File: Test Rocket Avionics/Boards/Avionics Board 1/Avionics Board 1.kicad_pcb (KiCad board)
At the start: 4 copper layers, 50 x 50 mm, 57 parts, among them J1 USB_A, J14 1S LiPo, J2 1S LiPo, M2.5 CHASSIS_GND, U1 ECS-.327-12.5-17X-TR, U2 SPX3819M5-L-3-3, U3 ATSAMD21G18, U4 MCP73831, U5 MPL3115A2, U6 DS3231-SO16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

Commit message: Update some stuff
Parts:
- added C20: 2.2u, Capacitors_SMD:C_1206, B.Cu at (44.4, 120.7)
- added C21: 1u, Capacitors_SMD:C_0805, F.Cu at (34.5, 123.1)
- added C22: 220p, Capacitors_SMD:C_0805, B.Cu at (44.0, 112.9)
- added C6: 2.2u, Capacitors_SMD:C_1206, B.Cu at (38.1, 117.5)
- added D6: D, Diodes_SMD:D_SOD-123F, B.Cu at (38.2, 120.4)
- added J3: EXPANSION_HEADER, Pin_Headers:Pin_Header_Straight_2x10_Pitch1.00mm, F.Cu at (24.2, 110.7)
- added J4: USB_A, Connectors:USB_Mini-B, B.Cu at (45.2, 84.9)
- added J5: SERVO, Pin_Headers:Pin_Header_Straight_1x03_Pitch2.54mm, F.Cu at (34.2, 119.9)
- added L1: 10u, Inductors_SMD:L_Wuerth_HCI-5040, B.Cu at (43.3, 124.6)
- added R17: 10k, Resistors_SMD:R_0805, B.Cu at (46.2, 117.5)
- added R18: 51k, Resistors_SMD:R_0805, B.Cu at (41.8, 113.0)
- added R19: 13.3k, Resistors_SMD:R_0805, B.Cu at (46.2, 114.0)
- added U10: NC7WZ07, TO_SOT_Packages_SMD:SOT-363_SC-70-6, F.Cu at (44.5, 111.1)
- added U11: LMR62014, TO_SOT_Packages_SMD:SOT-23-5, B.Cu at (42.8, 117.5)
- C14: value C -> 220p
- moved J2 54.2 mm to (29.4, 98.5), turned to 270 degrees
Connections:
- C14 pad 1: GND -> Net-(C14-Pad1)
- C14 pad 2: +3V3 -> /6V_SERVO_SUPPLY
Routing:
- net GND: track 80.8 -> 107.5 mm, vias 32 -> 34
- net /D13: track 0.00 -> 26.1 mm, vias 0 -> 1
- net /MISO: track 0.00 -> 23.0 mm
- net /D11: track 0.00 -> 22.6 mm, vias 0 -> 1
- net /SWCLK: track 6.41 -> 28.9 mm, vias 0 -> 2
- net /SWDIO: track 5.80 -> 26.7 mm, vias 0 -> 2
- net +3V3: track 54.3 -> 75.0 mm, vias 14 -> 16
- net /SCK: track 0.00 -> 19.8 mm, vias 0 -> 1
- net /MOSI: track 0.00 -> 18.6 mm
- net /6V_SERVO_SUPPLY: track 0.00 -> 18.1 mm
- net /A5: track 2.82 -> 20.0 mm, vias 0 -> 2
- net Net-(J5-Pad1): track 0.00 -> 16.3 mm
- net /A1: track 0.00 -> 11.2 mm, vias 0 -> 1
- net /D10: track 0.00 -> 9.32 mm
- net /A2: track 0.00 -> 8.78 mm, vias 0 -> 1
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
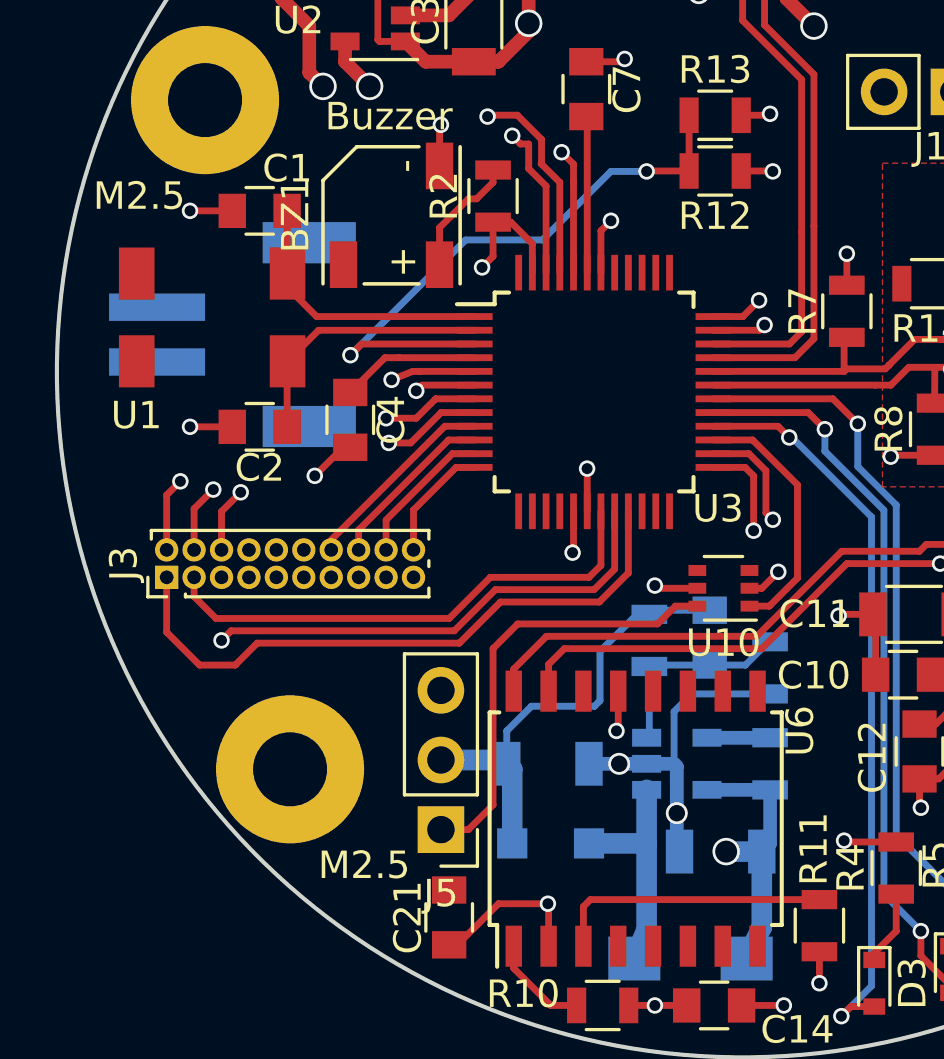
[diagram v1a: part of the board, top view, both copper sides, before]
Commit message: Connect JST connector to VBatt+ and GND nets
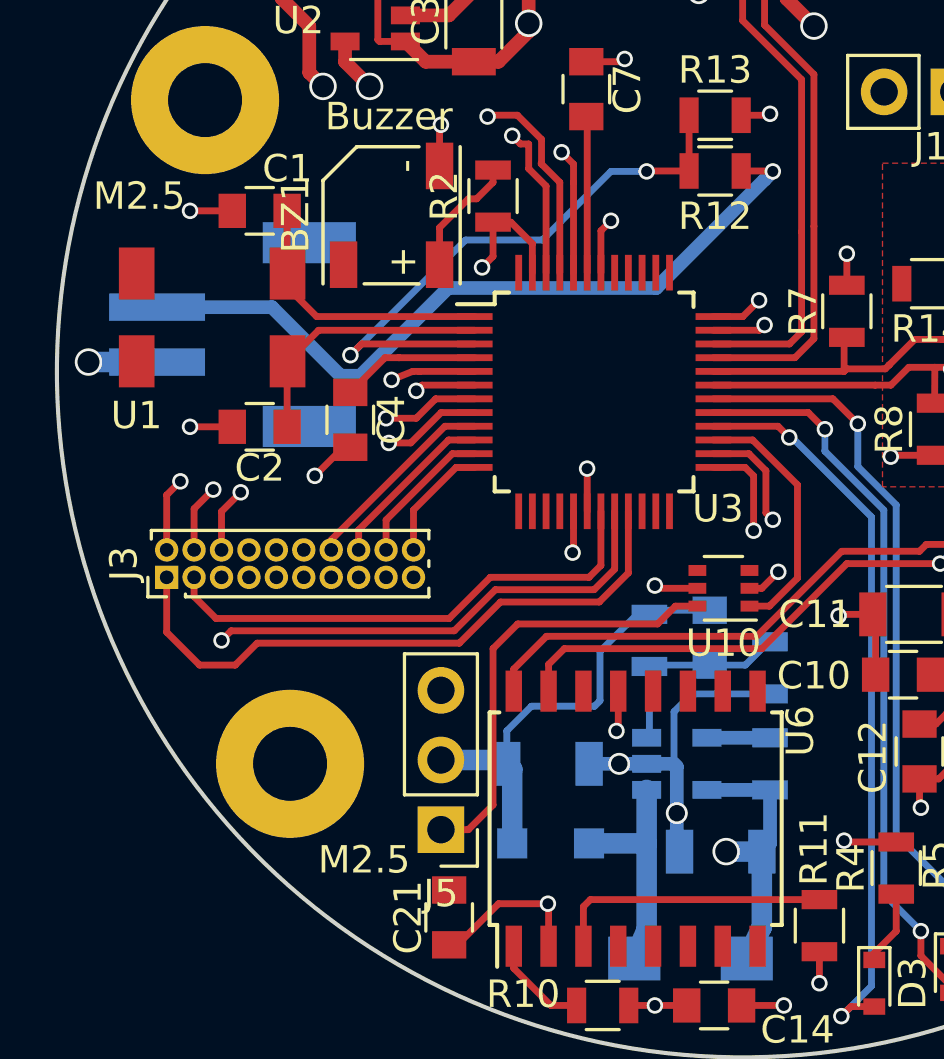
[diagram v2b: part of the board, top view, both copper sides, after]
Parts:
- moved M2.5 0.20 mm to (28.7, 117.5)
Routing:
- net +BATT: track 48.9 -> 75.5 mm
- net GND: track 107.5 -> 110.0 mm, vias 34 -> 35
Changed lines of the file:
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@@
-(kicad_pcb (version 4) (host pcbnew 4.0.7)
+(kicad_pcb (version 20171130) (host pcbnew "(5.1.0)-1")
   (general
-    (links 171)
-    (no_connects 11)
-    (area 20.163199 78.145199 70.316801 128.298801)
     (thickness 1.6)
-    (drawings 5)
-    (tracks 642)
+    (drawings 6)
+    (tracks 651)
     (zones 0)
     (modules 71)
@@
     (zone_45_only no)
     (trace_min 0.2)
-    (segment_width 0.2)
-    (edge_width 0.15)
     (via_size 0.6)
     (via_drill 0.4)
@@
     (uvia_min_size 0.2)
     (uvia_min_drill 0.1)
+    (edge_width 0.15)
+    (segment_width 0.2)
     (pcb_text_width 0.3)
     (pcb_text_size 1.5 1.5)
@@
       (layerselection 0x00030_80000001)
       (usegerberextensions false)
+      (usegerberattributes false)
+      (usegerberadvancedattributes false)
+      (creategerberjobfile false)
       (excludeedgelayer true)
       (linewidth 0.100000)
@@
       (hpglpennumber 1)
       (hpglpenspeed 20)
-      (hpglpendiameter 15)
-      (hpglpenoverlay 2)
+      (hpglpendiameter 15.000000)
       (psnegative false)
       (psa4output false)
@@
     (tags "USB USB_B USB_Mini connector")
     (attr smd)
-    (fp_text reference J1 (at 0 -5 360) (layer F.SilkS)
+    (fp_text reference J1 (at 0 -5) (layer F.SilkS)
       (effects (font (size 1 1) (thickness 0.15)))
     )
@@
   )
   (module Mounting_Holes:MountingHole_2.7mm_M2.5_Pad (layer F.Cu)
-    (at 28.74 117.722)
+    (at 28.74 117.522)
     (descr "Mounting Hole 2.7mm, M2.5")
     (tags "mounting hole 2.7mm m2.5")
@@
     (descr "Through hole straight pin header, 1x02, 2.54mm pitch, single row")
     (tags "Through hole pin header THT 1x02 2.54mm single row")
-    (fp_text reference J14 (at 2 0.4 360) (layer F.SilkS)
+    (fp_text reference J14 (at 2 0.4) (layer F.SilkS)
       (effects (font (size 1 1) (thickness 0.15)))
     )
@@
     (fp_line (start 1.8 4.35) (end 1.8 -1.8) (layer F.CrtYd) (width 0.05))
     (fp_line (start 1.8 -1.8) (end -1.8 -1.8) (layer F.CrtYd) (width 0.05))
-    (fp_text user %R (at 0 1.27 360) (layer F.Fab)
+    (fp_text user %R (at 0 1.27) (layer F.Fab)
       (effects (font (size 1 1) (thickness 0.15)))
     )
@@
   (module DannysLib:XC1195CT-ND (layer F.Cu)
     (at 58.852 106.366 270)
-    (fp_text reference U8 (at 6.096 2.54 360) (layer F.SilkS)
+    (fp_text reference U8 (at 6.096 2.54) (layer F.SilkS)
       (effects (font (size 1 1) (thickness 0.15)))
     )
-    (fp_text value ECS-.327-12.5-17X-TR (at 7.366 -1.778 360) (layer F.Fab)
+    (fp_text value ECS-.327-12.5-17X-TR (at 7.366 -1.778) (layer F.Fab)
       (effects (font (size 1 1) (thickness 0.15)))
     )
@@
     (at 44.94 103.922)
     (fp_text reference G*** (at 0 0) (layer B.SilkS) hide
-      (effects (font (thickness 0.3)) (justify mirror))
+      (effects (font (size 1.524 1.524) (thickness 0.3)) (justify mirror))
     )
     (fp_text value LOGO (at 0.75 0) (layer B.SilkS) hide
-      (effects (font (thickness 0.3)) (justify mirror))
+      (effects (font (size 1.524 1.524) (thickness 0.3)) (justify mirror))
     )
     (fp_poly (pts (xy -3.4036 -5.842) (xy -5.8928 -5.842) (xy -5.8928 -3.7084) (xy -5.5372 -3.7084)
@@
     (at 40.14 105.722 180)
     (fp_text reference G*** (at 0 0 180) (layer B.SilkS) hide
-      (effects (font (thickness 0.3)) (justify mirror))
+      (effects (font (size 1.524 1.524) (thickness 0.3)) (justify mirror))
     )
     (fp_text value LOGO (at 0.75 0 180) (layer B.SilkS) hide
-      (effects (font (thickness 0.3)) (justify mirror))
+      (effects (font (size 1.524 1.524) (thickness 0.3)) (justify mirror))
     )
     (fp_poly (pts (xy -9.867436 10.3378) (xy -10.460882 9.35358) (xy -11.225932 8.378132) (xy -12.132166 7.442081)
@@
   (module DannysLib:JST-PH2 (layer B.Cu)
     (at 29.44 98.522 270)
-    (fp_text reference J2 (at 6.5 6.5 540) (layer B.SilkS)
+    (fp_text reference J2 (at 6.5 6.5 180) (layer B.SilkS)
       (effects (font (size 1 1) (thickness 0.15)) (justify mirror))
     )
@@
       (effects (font (size 1 1) (thickness 0.15)))
     )
-    (fp_text value NC7WZ07 (at 0 2 360) (layer F.Fab)
+    (fp_text value NC7WZ07 (at 0 2) (layer F.Fab)
       (effects (font (size 1 1) (thickness 0.15)))
     )
@@
     )
   )
+  (dimension 39.3 (width 0.15) (layer Margin)
+    (gr_text "39.300 mm" (at 45.29 74.222) (layer Margin)
+      (effects (font (size 1 1) (thickness 0.15)))
+    )
+    (feature1 (pts (xy 64.94 93.322) (xy 64.94 74.935579)))
+    (feature2 (pts (xy 25.64 93.322) (xy 25.64 74.935579)))
+    (crossbar (pts (xy 25.64 75.522) (xy 64.94 75.522)))
+    (arrow1a (pts (xy 64.94 75.522) (xy 63.813496 76.108421)))
+    (arrow1b (pts (xy 64.94 75.522) (xy 63.813496 74.935579)))
+    (arrow2a (pts (xy 25.64 75.522) (xy 26.766504 76.108421)))
+    (arrow2b (pts (xy 25.64 75.522) (xy 26.766504 74.935579)))
+  )
   (gr_text "Danny Mallek 2019\n" (at 57.74 113.022) (layer B.SilkS)
     (effects (font (size 1 1) (thickness 0.1)) (justify mirror))
@@
   (segment (start 62.8655 100.9815) (end 63.424 101.54) (width 0.25) (layer F.Cu) (net 2))
   (segment (start 53.264 88.022) (end 53.24 88.022) (width 0.5) (layer F.Cu) (net 2) (status 30))
+  (via (at 21.39 102.872) (size 1) (drill 0.8) (layers F.Cu B.Cu) (net 2))
+  (segment (start 23.89 102.872) (end 21.39 102.872) (width 0.75) (layer B.Cu) (net 2))
   (segment (start 35.474 101.214) (end 29.708 101.214) (width 0.25) (layer F.Cu) (net 3))
   (segment (start 29.708 101.214) (end 28.648 100.154) (width 0.25) (layer F.Cu) (net 3))
@@
   (segment (start 60.924 85.606) (end 59.84 84.522) (width 0.5) (layer F.Cu) (net 10))
   (segment (start 59.84 84.522) (end 58.84 83.522) (width 0.5) (layer F.Cu) (net 10))
+  (segment (start 42.089999 100.172001) (end 46.040001 96.221999) (width 0.5) (layer B.Cu) (net 10))
+  (segment (start 34.500001 100.172001) (end 42.089999 100.172001) (width 0.5) (layer B.Cu) (net 10))
+  (segment (start 31.300001 103.372001) (end 34.500001 100.172001) (width 0.5) (layer B.Cu) (net 10))
+  (segment (start 30.579999 103.372001) (end 31.300001 103.372001) (width 0.5) (layer B.Cu) (net 10))
+  (segment (start 46.040001 96.221999) (end 46.34 95.922) (width 0.5) (layer B.Cu) (net 10))
+  (segment (start 28.079998 100.872) (end 30.579999 103.372001) (width 0.5) (layer B.Cu) (net 10))
+  (segment (start 23.89 100.872) (end 28.079998 100.872) (width 0.5) (layer B.Cu) (net 10))
   (segment (start 60.146 98.669) (end 60.146 96.69) (width 0.25) (layer F.Cu) (net 11))
   (segment (start 60.376 96.46) (end 60.376 95.428) (width 0.25) (layer F.Cu) (net 11))
